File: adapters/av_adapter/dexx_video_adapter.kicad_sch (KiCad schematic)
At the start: 6 parts, among them J1 SCART-F, J2 Pr, J3 Y, J4 Pb, J5 AudioJack3, J6 DB15_Female_HighDensity

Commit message: update av_adapter board to v1.1
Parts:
- added MH1, MH2: MountingHole, MountingHole:MountingHole_3.2mm_M3_ISO14580_Pad, symbol Mechanical:MountingHole
- added R1: 500, custom_components:SM0603_Resistor_libcms, symbol Device:R
- added R2: 180, custom_components:SM0603_Resistor_libcms, symbol Device:R
- added SW1: SW_SPDT, custom_components:SWITCH_11MA1QS1, symbol Switch:SW_SPDT
- J5: footprint custom_components:SJ1-3533NG -> Connector_Audio:Jack_3.5mm_CUI_SJ1-3533NG_Horizontal
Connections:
- net AV_S: now also SW1.3 (C); no longer J6.4
- net GND: now also R1.2
- net AV_RGB_STATUS: now reaches J1.16 (P16)
- net AV_RGB_STATUS: now also R2.1
- net AV_S_OUT: now reaches J1.19 (P19)
- net AV_S_OUT: now also SW1.1 (A)
- net DDC_5V: now reaches J6.9
- net DDC_5V: now also R1.1, R2.2
- new net AV_S_SEL: J6.4, SW1.2 (B)
- no-connect marks 7 -> 4
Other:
- title: DExx AV adapter -> AV adapter
- moved on the sheet: J2, J3, J4, J5, J6

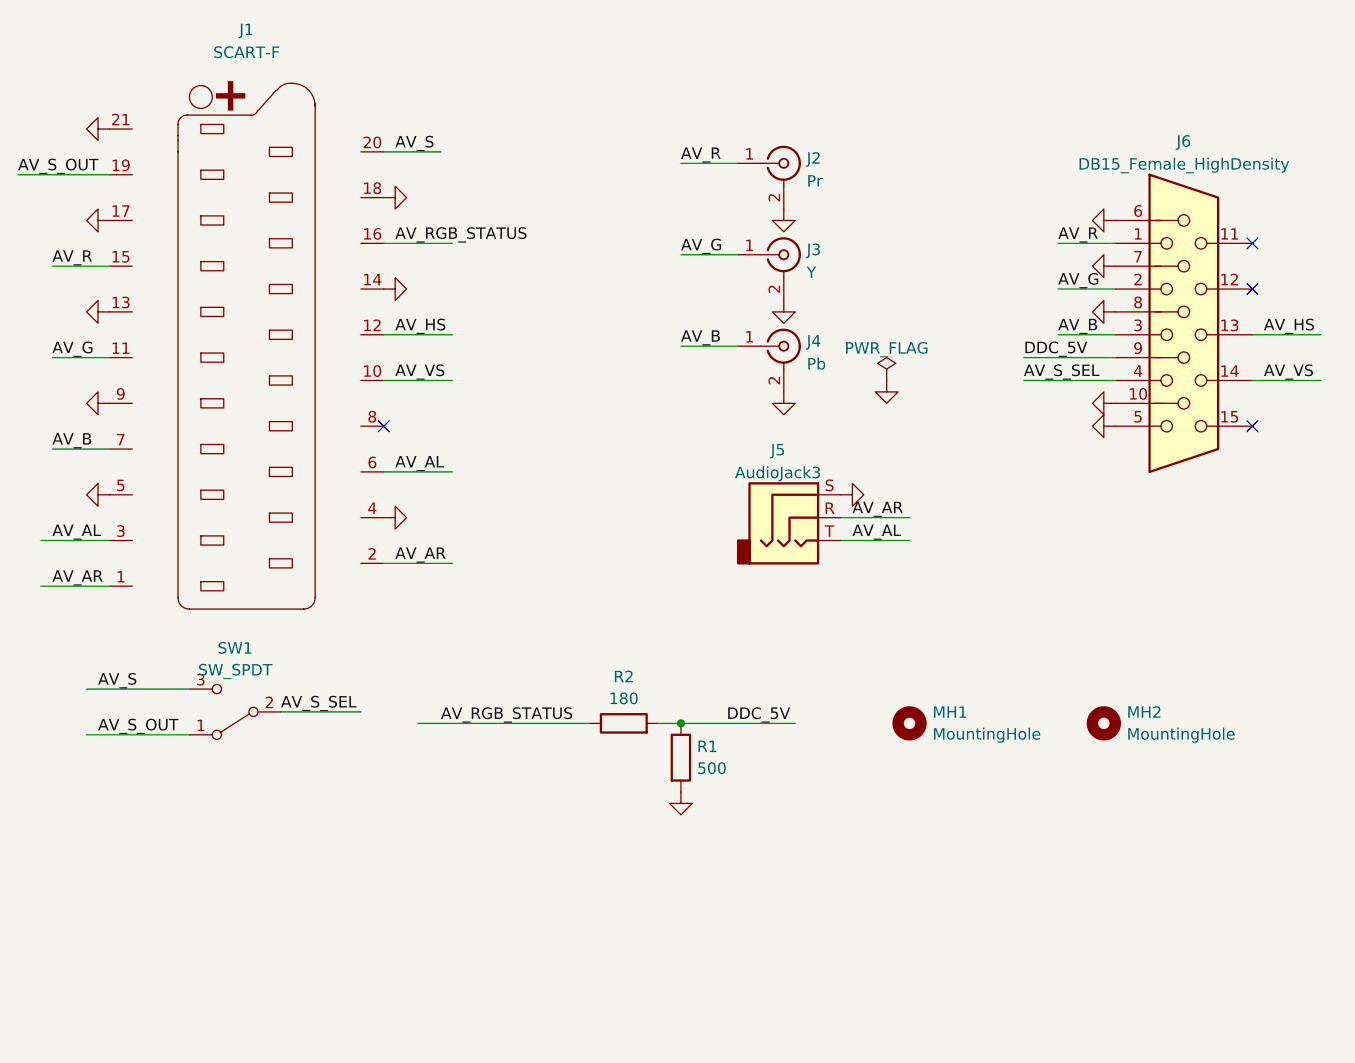
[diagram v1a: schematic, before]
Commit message: update av_adapter to v1.2
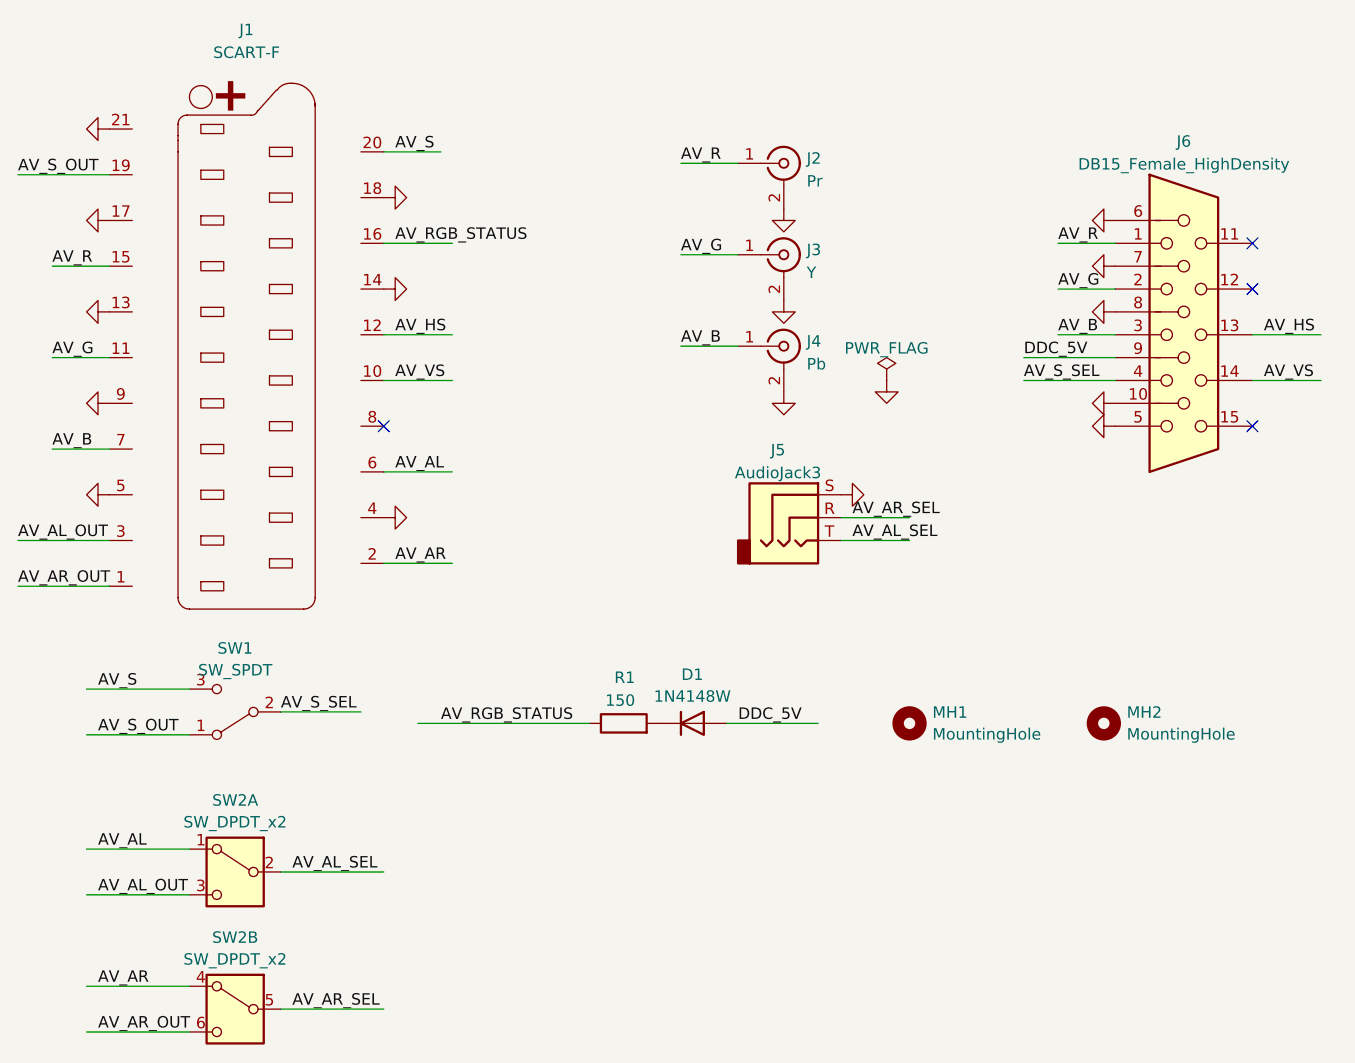
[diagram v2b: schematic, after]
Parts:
- removed R2: 180, custom_components:SM0603_Resistor_libcms, symbol Device:R
- added D1: 1N4148W, Diode_SMD:D_SOD-123, symbol Diode:1N4148W
- added SW2: SW_DPDT_x2, custom_components:SW6_OS202011MA0QS1_CNK, symbol Switch:SW_DPDT_x2
- R1: value 500 -> 150
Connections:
- net AV_AL: now also SW2.1 (A); no longer J1.3 (P3), J5.T
- net AV_AR: now also SW2.4 (A); no longer J1.1 (P1), J5.R
- net AV_RGB_STATUS: now also R1.1
- net DDC_5V: now also D1.2 (A); no longer R1.1
- net GND: no longer R1.2
- new net: D1.1 (K), R1.2
- new net AV_AL_OUT: J1.3 (P3), SW2.3 (C)
- new net AV_AL_SEL: J5.T, SW2.2 (B)
- new net AV_AR_OUT: J1.1 (P1), SW2.6 (C)
- new net AV_AR_SEL: J5.R, SW2.5 (B)
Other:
- moved on the sheet: R1

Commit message: update av_adapter to v1.3
* add compatibility mode for VGA cables with pin 4 missing or grounded
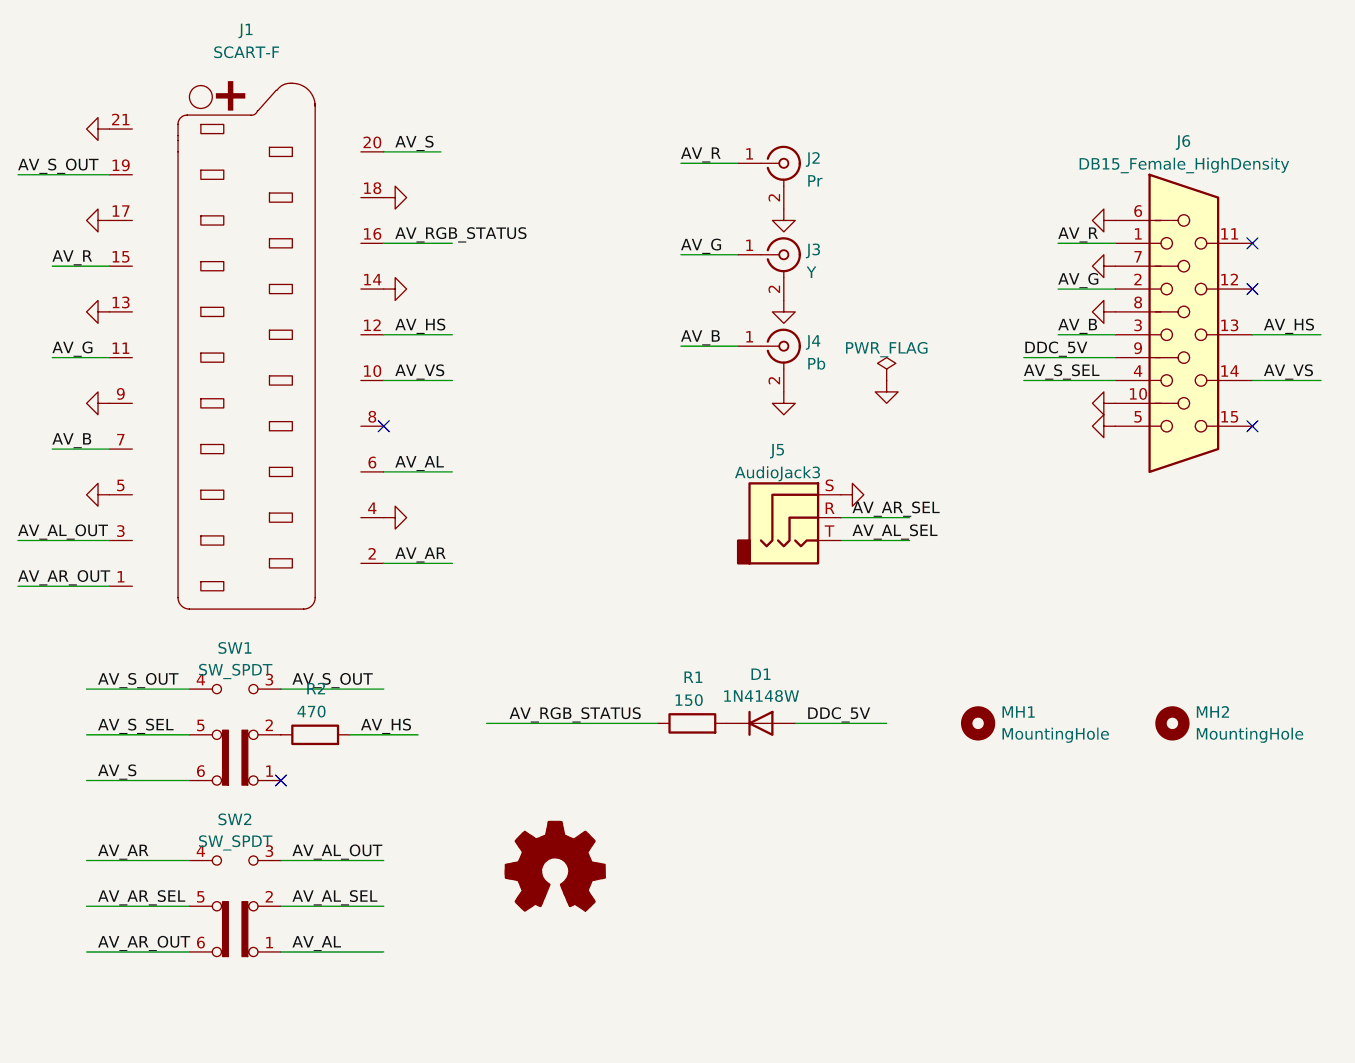
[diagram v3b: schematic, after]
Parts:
- removed SW2: SW_DPDT_x2, custom_components:SW6_OS202011MA0QS1_CNK, symbol Switch:SW_DPDT_x2
- added R2: 470, custom_components:SM0603_Resistor_libcms, symbol Device:R
- added SW2: SW_SPDT, custom_components:SW6_OS202011MA0QS1_CNK, symbol Switch:SW_Slide_DPDT
- added SYM1: Logo_Open_Hardware_Small, Symbol:WEEE-Logo_4.2x6mm_SilkScreen, symbol Graphic:Logo_Open_Hardware_Small
- SW1: footprint custom_components:SWITCH_11MA1QS1 -> custom_components:SW6_OS202011MA0QS1_CNK; symbol Switch:SW_SPDT -> Switch:SW_Slide_DPDT
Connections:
- net AV_AL: now also SW2.1 (A)
- net AV_AL_OUT: now also SW2.3 (C)
- net AV_AL_SEL: now also SW2.2 (B)
- net AV_AR: now also SW2.4 (A)
- net AV_AR_OUT: now also SW2.6 (C)
- net AV_AR_SEL: now also SW2.5 (B)
- net AV_HS: now also R2.2
- net AV_S: now also SW1.6 (C); no longer SW1.3 (C)
- net AV_S_OUT: now also SW1.3 (C), SW1.4 (A); no longer SW1.1 (A)
- net AV_S_SEL: now also SW1.5 (B); no longer SW1.2 (B)
- new net: R2.1, SW1.2 (B)
- no-connect marks 4 -> 5
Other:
- moved on the sheet: D1, MH1, MH2, R1
